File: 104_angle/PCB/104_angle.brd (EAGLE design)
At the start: 25.4 x 33 mm, 4 parts

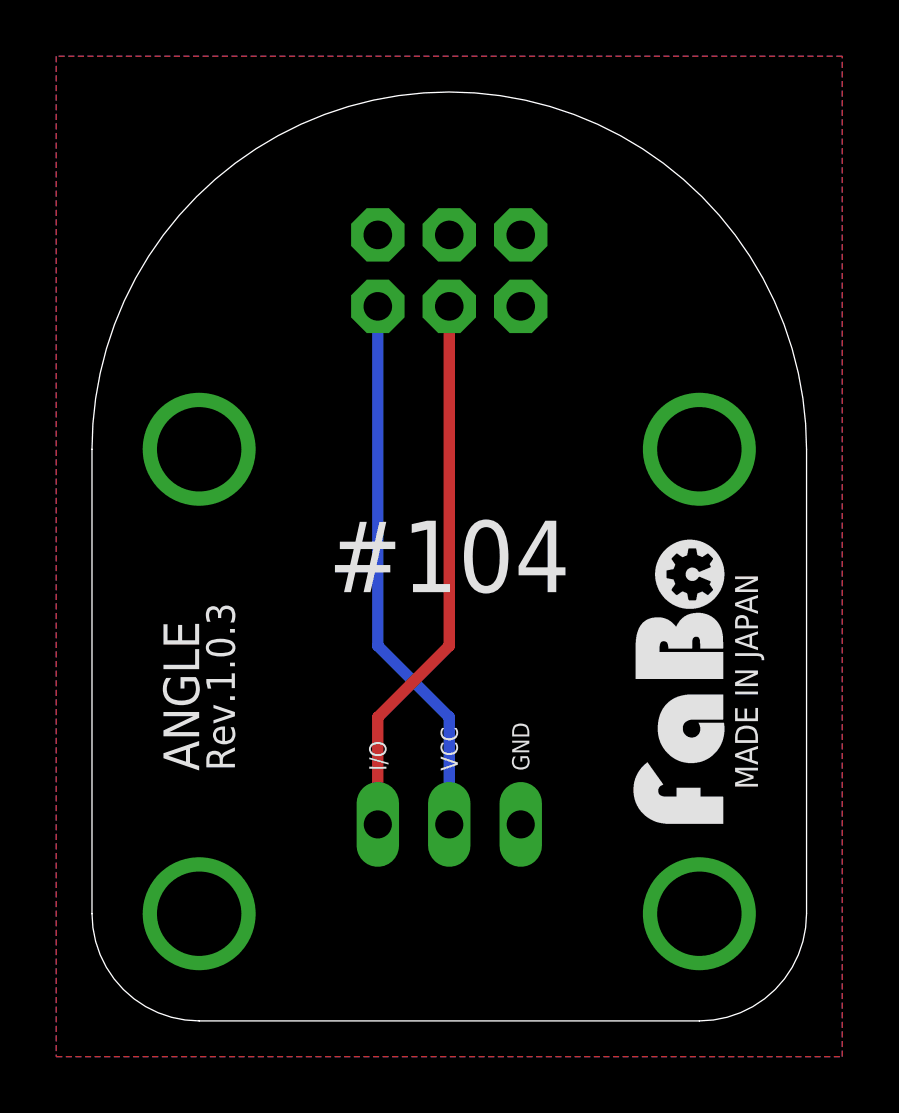
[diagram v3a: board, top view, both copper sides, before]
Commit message: change jst connector
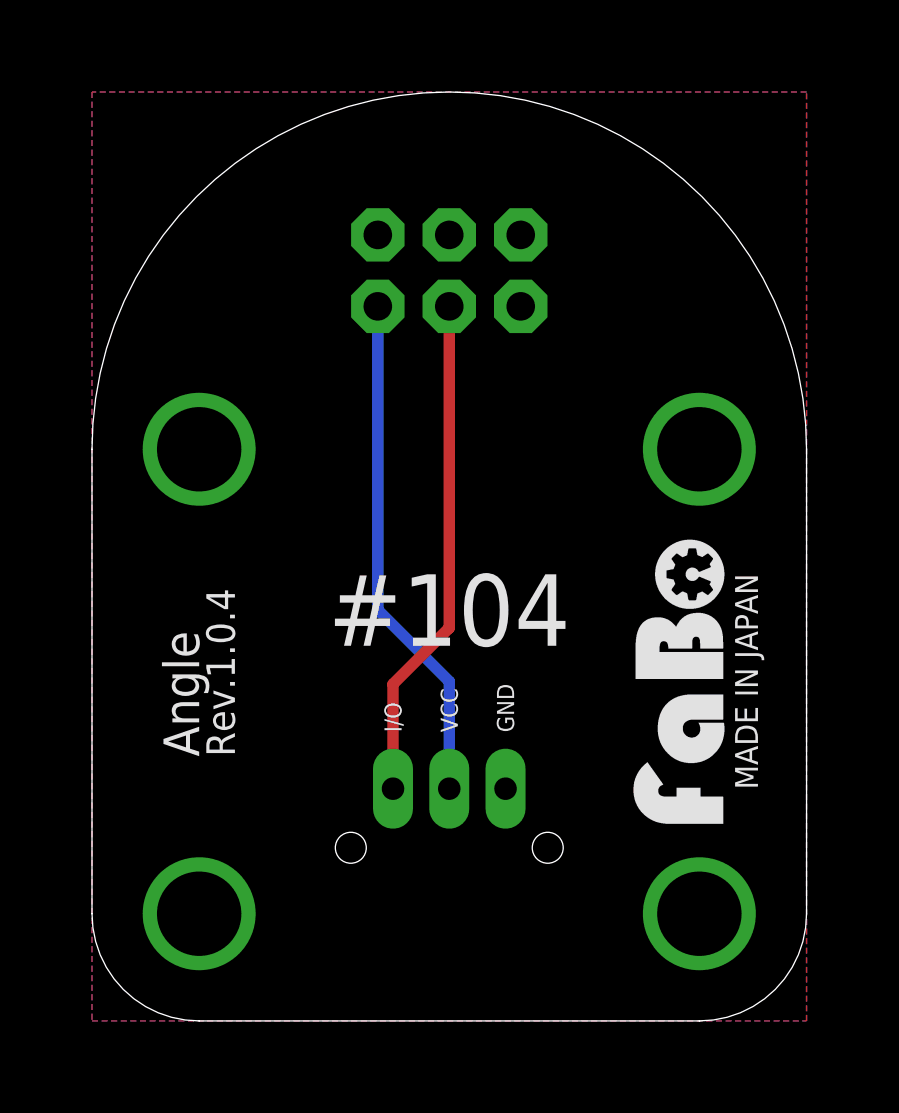
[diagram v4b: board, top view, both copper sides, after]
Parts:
- U$3: device FaBo-etc:LOGO_OSHW_T_MS_BOTTOM -> FaBo-etc:LOGO_OSHW_M_BOTTOM
- moved U$3 0.25 mm to (12.7, 3.17)
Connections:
- net N$1: now also J1.I/O; no longer J1.IN/OUT
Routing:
- net N$1: track 19.5 -> 18.0 mm
- net VCC: track 19.5 -> 18.2 mm
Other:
- board text added: "Angle"
- board text added: "Rev.1.0.4"
- board text removed: "ANGLE"
- board text removed: "Rev.1.0.3"
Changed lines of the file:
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@@
 <?xml version="1.0" encoding="utf-8"?>
 <!DOCTYPE eagle SYSTEM "eagle.dtd">
-<eagle version="7.5.0">
+<eagle version="7.6.0">
 <drawing>
 <settings>
@@
 <layer number="50" name="dxf" color="7" fill="1" visible="no" active="yes"/>
 <layer number="51" name="tDocu" color="14" fill="1" visible="yes" active="yes"/>
-<layer number="52" name="bDocu" color="7" fill="1" visible="yes" active="yes"/>
+<layer number="52" name="bDocu" color="7" fill="1" visible="no" active="yes"/>
 <layer number="53" name="tGND_GNDA" color="7" fill="9" visible="no" active="no"/>
 <layer number="54" name="bGND_GNDA" color="1" fill="9" visible="no" active="no"/>
 <layer number="56" name="wert" color="7" fill="1" visible="no" active="yes"/>
 <layer number="57" name="tCAD" color="7" fill="1" visible="no" active="no"/>
+<layer number="59" name="tCarbon" color="7" fill="1" visible="no" active="no"/>
+<layer number="60" name="bCarbon" color="7" fill="1" visible="no" active="no"/>
 <layer number="90" name="Modules" color="5" fill="1" visible="no" active="no"/>
 <layer number="91" name="Nets" color="2" fill="1" visible="no" active="no"/>
@@
 <layer number="109" name="fp9" color="7" fill="1" visible="no" active="yes"/>
 <layer number="110" name="fp0" color="7" fill="1" visible="no" active="yes"/>
-<layer number="111" name="LPC17xx" color="7" fill="1" visible="yes" active="yes"/>
+<layer number="111" name="LPC17xx" color="7" fill="1" visible="no" active="yes"/>
 <layer number="112" name="tSilk" color="7" fill="1" visible="yes" active="yes"/>
 <layer number="113" name="IDFDebug" color="4" fill="1" visible="yes" active="yes"/>
 <layer number="116" name="Patch_BOT" color="9" fill="4" visible="no" active="yes"/>
+<layer number="118" name="Rect_Pads" color="7" fill="1" visible="no" active="no"/>
 <layer number="121" name="_tsilk" color="7" fill="1" visible="no" active="yes"/>
 <layer number="122" name="_bsilk" color="7" fill="1" visible="no" active="yes"/>
@@
 <layer number="127" name="_tValues" color="7" fill="1" visible="yes" active="yes"/>
 <layer number="128" name="_bValues" color="7" fill="1" visible="yes" active="yes"/>
+<layer number="129" name="Mask" color="7" fill="1" visible="yes" active="yes"/>
 <layer number="131" name="tAdjust" color="7" fill="1" visible="no" active="yes"/>
 <layer number="132" name="bAdjust" color="7" fill="1" visible="no" active="yes"/>
@@
 <layer number="223" name="223bmp" color="24" fill="1" visible="no" active="no"/>
 <layer number="224" name="224bmp" color="25" fill="1" visible="no" active="no"/>
+<layer number="225" name="225bmp" color="7" fill="1" visible="yes" active="yes"/>
+<layer number="226" name="226bmp" color="7" fill="1" visible="yes" active="yes"/>
+<layer number="227" name="227bmp" color="7" fill="1" visible="yes" active="yes"/>
+<layer number="228" name="228bmp" color="7" fill="1" visible="yes" active="yes"/>
+<layer number="229" name="229bmp" color="7" fill="1" visible="yes" active="yes"/>
+<layer number="230" name="230bmp" color="7" fill="1" visible="yes" active="yes"/>
+<layer number="231" name="Eagle3D_PG1" color="7" fill="1" visible="no" active="no"/>
+<layer number="232" name="Eagle3D_PG2" color="7" fill="1" visible="no" active="no"/>
+<layer number="233" name="Eagle3D_PG3" color="7" fill="1" visible="no" active="no"/>
 <layer number="248" name="Housing" color="7" fill="1" visible="yes" active="yes"/>
 <layer number="249" name="Edge" color="7" fill="1" visible="yes" active="yes"/>
@@
 <layer number="251" name="SMDround" color="12" fill="11" visible="no" active="no"/>
 <layer number="254" name="cooling" color="7" fill="1" visible="no" active="yes"/>
+<layer number="255" name="routoute" color="7" fill="1" visible="no" active="yes"/>
 </layers>
 <board>
 <plain>
-<text x="3.81" y="8.89" size="1.27" layer="21" font="vector" ratio="12" rot="R90">ANGLE</text>
-<text x="5.08" y="8.89" size="1.016" layer="21" font="vector" ratio="12" rot="R90">Rev.1.0.3</text>
+<text x="3.81" y="9.398" size="1.27" layer="21" font="vector" ratio="12" rot="R90">Angle</text>
+<text x="5.08" y="9.398" size="1.016" layer="21" font="vector" ratio="12" rot="R90">Rev.1.0.4</text>
 <text x="22.86" y="12.065" size="0.8128" layer="21" font="vector" ratio="12" rot="R270" align="bottom-center">MADE IN JAPAN</text>
-<text x="12.7" y="16.51" size="2.54" layer="21" font="vector" ratio="12" align="center">#104</text>
+<text x="12.7" y="13.335" size="2.54" layer="21" font="vector" ratio="12" align="bottom-center">#104</text>
 </plain>
 <attributes>
@@
 </class>
 </classes>
-<designrules name="Elecrow_2-layer_eagle_rule">
+<designrules name="SeeedStudio_2layer_DRU_no_angle_20140221">
 <description language="de">&lt;b&gt;EAGLE Design Rules&lt;/b&gt;
 &lt;p&gt;
@@
 necessary adjustments and save your customized
 design rules under a new name.</description>
-<description language="zh">&lt;b&gt;Elecrow EAGLE Design Rules&lt;/b&gt;
+<description language="zh">&lt;b&gt;Seeed Studio EAGLE Design Rules&lt;/b&gt;
 </description>
 <param name="layerSetup" value="(1*16)"/>
-<param name="mtCopper" value="0.035mm 0.035mm 0.035mm 0.035mm 0.035mm 0.035mm 0.035mm 0.035mm 0.035mm 0.035mm 0.035mm 0.035mm 0.035mm 0.035mm 0.035mm 0.035mm"/>
-<param name="mtIsolate" value="1.5mm 0.15mm 0.2mm 0.15mm 0.2mm 0.15mm 0.2mm 0.15mm 0.2mm 0.15mm 0.2mm 0.15mm 0.2mm 0.15mm 0.2mm"/>
+<param name="mtCopper" value="0.035mm 0.0175mm 0.035mm 0.035mm 0.035mm 0.035mm 0.035mm 0.035mm 0.035mm 0.035mm 0.035mm 0.035mm 0.035mm 0.035mm 0.0175mm 0.035mm"/>
+<param name="mtIsolate" value="1.5mm 1.1mm 0.2mm 0.15mm 0.2mm 0.15mm 0.2mm 0.15mm 0.2mm 0.15mm 0.2mm 0.15mm 0.2mm 0.15mm 0.2mm"/>
 <param name="mdWireWire" value="6mil"/>
 <param name="mdWirePad" value="6mil"/>
@@
 <element name="J1" library="FaBo-Template" package="FABO_BRICK_3PIN" value="" x="12.7" y="16.51"/>
 <element name="U$2" library="FaBo-etc" package="LOGO_FABO_MS" value="" x="22.86" y="12.065" rot="R90"/>
-<element name="U$3" library="FaBo-etc" package="LOGO_OSHW_T_MS_BOTTOM" value="" x="12.7" y="3.429"/>
 <element name="U1" library="FaBo-Parts" package="ROTARYENCORDER" value="" x="12.7" y="26.67"/>
+<element name="U$3" library="FaBo-etc" package="LOGO_OSHW_M_BOTTOM" value="" x="12.7" y="3.175"/>
 </elements>
 <signals>
+<signal name="N$1">
+<contactref element="J1" pad="I/O"/>
+<contactref element="U1" pad="3"/>
+<wire x1="12.7" y1="25.4" x2="12.7" y2="13.97" width="0.4064" layer="1"/>
+<wire x1="10.7" y1="8.255" x2="10.7" y2="11.97" width="0.4064" layer="1"/>
+<wire x1="10.7" y1="11.97" x2="12.7" y2="13.97" width="0.4064" layer="1"/>
+</signal>
 <signal name="VCC">
 <contactref element="J1" pad="VCC"/>
 <contactref element="U1" pad="1"/>
-<wire x1="10.16" y1="25.4" x2="10.16" y2="13.335" width="0.4064" layer="16"/>
-<wire x1="10.16" y1="13.335" x2="12.7" y2="10.795" width="0.4064" layer="16"/>
-<wire x1="12.7" y1="10.795" x2="12.7" y2="6.985" width="0.4064" layer="16"/>
+<wire x1="10.16" y1="25.4" x2="10.16" y2="14.605" width="0.4064" layer="16"/>
+<wire x1="12.7" y1="8.255" x2="12.7" y2="12.065" width="0.4064" layer="16"/>
+<wire x1="12.7" y1="12.065" x2="10.16" y2="14.605" width="0.4064" layer="16"/>
 </signal>
 <signal name="GND">
 <contactref element="J1" pad="GND"/>
 <contactref element="U1" pad="5"/>
-<polygon width="0.2032" layer="16" spacing="0.254">
-<vertex x="-1.27" y="-1.27"/>
-<vertex x="26.67" y="-1.27"/>
-<vertex x="26.67" y="34.29"/>
-<vertex x="-1.27" y="34.29"/>
+<polygon width="0.1524" layer="16" spacing="0.1524">
+<vertex x="0" y="0"/>
+<vertex x="25.4" y="0"/>
+<vertex x="25.4" y="33.02"/>
+<vertex x="0" y="33.02"/>
 </polygon>
-<polygon width="0.2032" layer="1" spacing="0.254">
-<vertex x="-1.27" y="-1.27"/>
-<vertex x="26.67" y="-1.27"/>
-<vertex x="26.67" y="34.29"/>
-<vertex x="-1.27" y="34.29"/>
+<polygon width="0.1524" layer="1" spacing="0.1524">
+<vertex x="0" y="0"/>
+<vertex x="25.4" y="0"/>
+<vertex x="25.4" y="33.02"/>
+<vertex x="0" y="33.02"/>
 </polygon>
 </signal>
-<signal name="N$1">
-<contactref element="J1" pad="IN/OUT"/>
-<contactref element="U1" pad="3"/>
-<wire x1="12.7" y1="25.4" x2="12.7" y2="13.335" width="0.4064" layer="1"/>
-<wire x1="12.7" y1="13.335" x2="10.16" y2="10.795" width="0.4064" layer="1"/>
-<wire x1="10.16" y1="10.795" x2="10.16" y2="6.985" width="0.4064" layer="1"/>
-</signal>
 </signals>
